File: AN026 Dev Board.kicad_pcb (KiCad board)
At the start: 2 copper layers, 5 parts, among them J1 Conn_01x19_Pin, J2 Conn_01x19_Pin

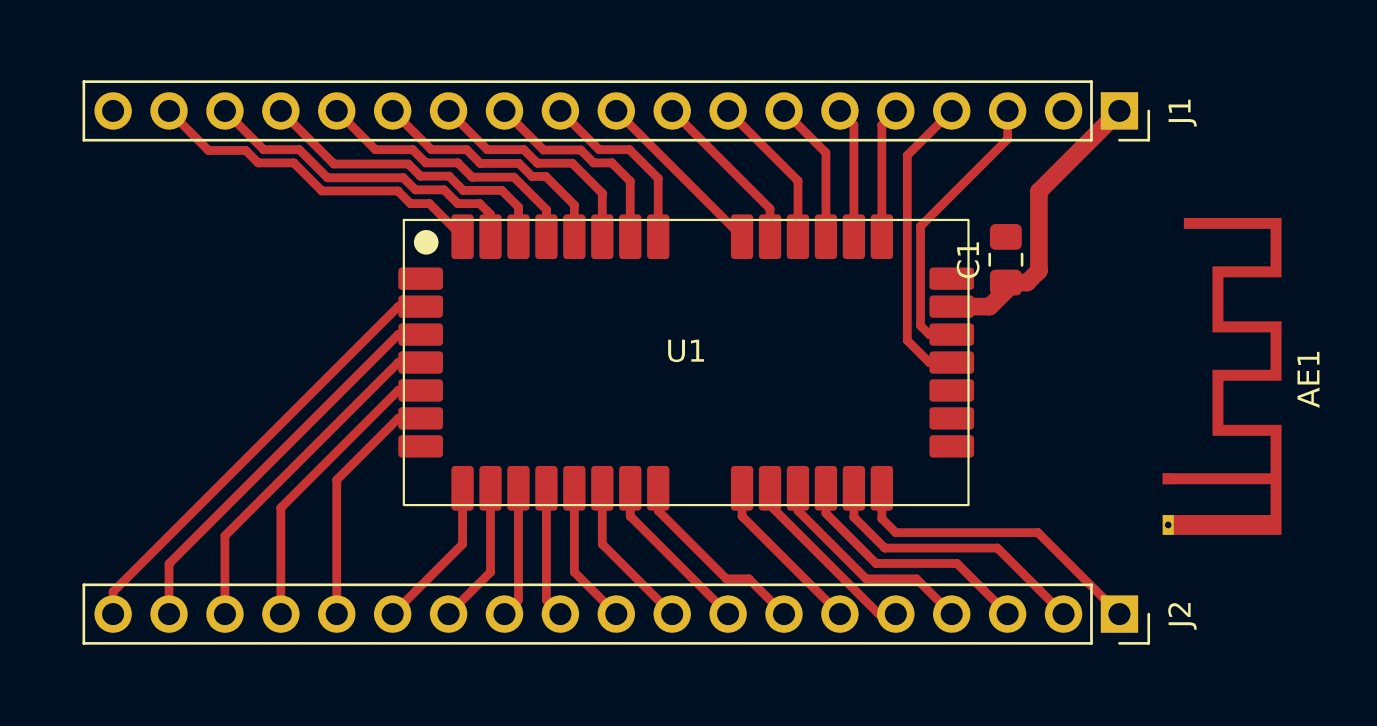
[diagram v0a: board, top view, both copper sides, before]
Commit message: Finished up the PCB.
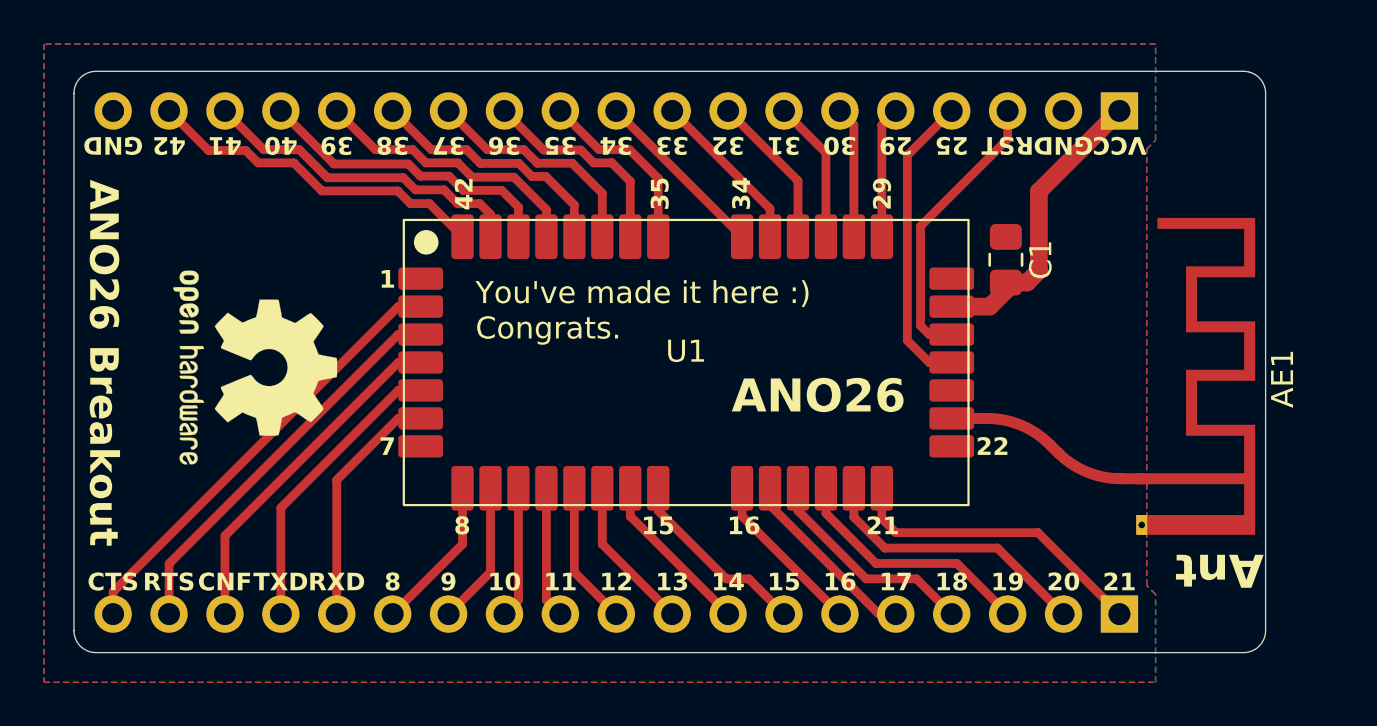
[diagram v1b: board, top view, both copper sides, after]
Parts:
- added REF**: OSHW-Logo2_9.8x8mm_SilkScreen, Symbol:OSHW-Logo2_9.8x8mm_SilkScreen, F.Cu at (110.6, 77.7)
- added REF**: KiCad-Logo2_6mm_SilkScreen, Symbol:KiCad-Logo2_6mm_SilkScreen, B.Cu at (151.5, 76.7)
- added REF**: OSHW-Logo2_14.6x12mm_SilkScreen, Symbol:OSHW-Logo2_14.6x12mm_SilkScreen, B.Cu at (108.2, 77.5)
- J1, J2: footprint Connector_PinSocket_2.54mm:PinSocket_1x19_P2.54mm_Vertical -> Connector_PinHeader_2.54mm:PinHeader_1x19_P2.54mm_Vertical; moved to B.Cu
- moved AE1 1.20 mm to (150.9, 82.8)
- turned J1 to 90 degrees
- turned J2 to 90 degrees
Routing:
- net Net-(AE1-FEED): track 0.00 -> 9.39 mm
- added copper zone on B.Cu, net GND
- added copper zone on F.Cu, net GND
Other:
- board outline added: 54.1 x 26.4 mm
- board text added: "1"
- board text added: "10"
- board text added: "11"
- board text added: "12"
- board text added: "13"
- board text added: "14"
- board text added: "15"
- board text added: "16"
- board text added: "17"
- board text added: "18"
- board text added: "19"
- board text added: "20"
- board text added: "21"
- board text added: "22"
- board text added: "25"
- board text added: "29"
- board text added: "30"
- board text added: "31"
- board text added: "32"
- board text added: "33"
- board text added: "34"
- board text added: "35"
- board text added: "36"
- board text added: "37"
- board text added: "38"
- board text added: "39"
- board text added: "40"
- board text added: "41"
- board text added: "42"
- board text added: "7"
- board text added: "8"
- board text added: "9"
- board text added: "ANO26"
- board text added: "ANO26 Breakout"
- board text added: "Ant"
- board text added: "CNF"
- board text added: "CTS"
- board text added: "GND"
- board text added: "Made by: Tomas Kuchta"
- board text added: "RST"
- board text added: "RTS"
- board text added: "RXD"
- board text added: "TXD"
- board text added: "VCC"
- board text added: "You've made it here :) Congrats."

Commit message: Its AN026 not ANO26.
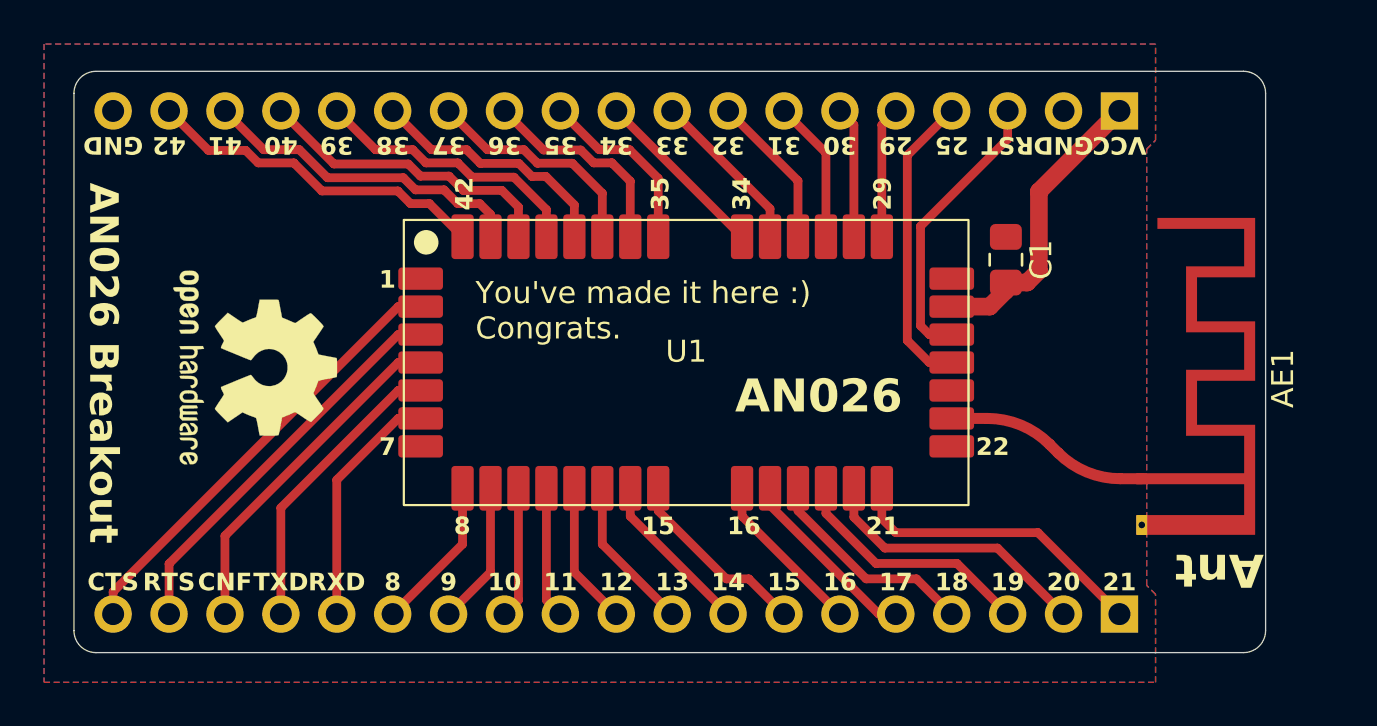
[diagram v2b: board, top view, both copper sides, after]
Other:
- board text added: "AN026"
- board text added: "AN026 Breakout"
- board text removed: "ANO26"
- board text removed: "ANO26 Breakout"
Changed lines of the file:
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@@
 		(tags "Through hole pin header THT 1x19 2.54mm single row")
 		(property "Reference" "J1"
-			(at 0 2.38 -90)
+			(at 0 2.38 270)
 			(layer "B.SilkS")
 			(effects
@@
 		)
 		(property "Value" "Conn_01x19_Pin"
-			(at 0 -48.1 -90)
+			(at 0 -48.1 270)
 			(layer "B.Fab")
 			(effects
@@
 		)
 		(property "Datasheet" "~"
-			(at 0 0 -90)
+			(at 0 0 270)
 			(layer "B.Fab")
 			(hide yes)
@@
 		)
 		(property "Description" "Generic connector, single row, 01x19, script generated"
-			(at 0 0 -90)
+			(at 0 0 270)
 			(layer "B.Fab")
 			(hide yes)
@@
 		(tags "Through hole pin header THT 1x19 2.54mm single row")
 		(property "Reference" "J2"
-			(at 0 2.38 -90)
+			(at 0 2.38 270)
 			(layer "B.SilkS")
 			(effects
@@
 		)
 		(property "Value" "Conn_01x19_Pin"
-			(at 0 -48.1 -90)
+			(at 0 -48.1 270)
 			(layer "B.Fab")
 			(effects
@@
 		)
 		(property "Datasheet" "~"
-			(at 0 0 -90)
+			(at 0 0 270)
 			(layer "B.Fab")
 			(hide yes)
@@
 		)
 		(property "Description" "Generic connector, single row, 01x19, script generated"
-			(at 0 0 -90)
+			(at 0 0 270)
 			(layer "B.Fab")
 			(hide yes)
@@
 		)
 	)
-	(gr_text "ANO26"
+	(gr_text "AN026"
 		(at 136.2 79 0)
 		(layer "F.SilkS")
@@
 		)
 	)
-	(gr_text "ANO26 Breakout"
+	(gr_text "AN026 Breakout"
 		(at 103.7 77.5 270)
 		(layer "F.SilkS")
@@
 		)
 	)
-	(gr_text "ANO26"
+	(gr_text "AN026"
 		(at 133 77.47 0)
 		(layer "B.SilkS")
